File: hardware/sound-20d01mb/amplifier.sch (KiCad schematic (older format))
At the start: 49 parts

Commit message: Added AD1938
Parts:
- removed C?: 10uF, Capacitor_SMD:CP_Elec_4x5.4, symbol Device:CP
- removed C? (x5): 0.1uF, Capacitor_SMD:C_1206_3216Metric_Pad1.42x1.75mm_HandSolder, symbol Device:C
- removed C? (x2): 10uF, Capacitor_THT:CP_Radial_D8.0mm_P3.50mm, symbol Device:CP
- removed R?: 100K, Resistor_SMD:R_1206_3216Metric_Pad1.42x1.75mm_HandSolder, symbol Device:R
- removed R? (x2): 100R, Resistor_SMD:R_1206_3216Metric_Pad1.42x1.75mm_HandSolder, symbol Device:R
- removed R? (x2): 10K, Resistor_SMD:R_1206_3216Metric_Pad1.42x1.75mm_HandSolder, symbol Device:R
- removed U?: PGA2311P, Package_DIP:DIP-16_W7.62mm, symbol sound-20d01_Library:PGA2311P
- removed U?: ADG3304BRUZ, Package_SO:TSSOP-14_4.4x5mm_P0.65mm, symbol sound-20d01_Library:ADG3304BRUZ
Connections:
- net labels removed: +3.3V, +5V, +5VA, -5VA, PGA_SCLK, PGA_SDI, PGA_ZCEN, VOL_SCLK, VOL_SDI, VOL_ZCEN, ~PGA_CS, ~VOL_CS
- wire segments 229 -> 145
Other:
- note removed: "Place power-supply bypass capacitors as\nclose to the PGA2311 package as physically possible."
- moved on the sheet: C?, L?, R?, SW?, U?

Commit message: Updated schematics
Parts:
- removed C?: 10uF, Capacitor_THT:CP_Radial_D8.0mm_P3.50mm, symbol Device:CP
- removed R? (x2): 100R, Resistor_SMD:R_1206_3216Metric_Pad1.42x1.75mm_HandSolder, symbol Device:R
- removed R? (x2): 1M, Resistor_SMD:R_1206_3216Metric_Pad1.42x1.75mm_HandSolder, symbol Device:R
- added C?: 10uF, Capacitor_SMD:C_1210_3225Metric_Pad1.42x2.65mm_HandSolder, symbol Device:C
- C?: value 1uF -> 2.2uF
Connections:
- net GNDA: now also C?.2
- net LIN: now also C?.1
- net RIN: now also C?.1
- net VCC: now also C?.1
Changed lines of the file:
@@
 	5750 3800 5750 4700
-$Comp
-L Device:CP C?
-U 1 1 60E1A09F
-P 6850 2850
-F 0 "C?" H 6968 2896 50  0000 L CNN
-F 1 "10uF" H 6968 2805 50  0000 L CNN
-F 2 "Capacitor_THT:CP_Radial_D8.0mm_P3.50mm" H 6888 2700 50  0001 C CNN
-F 3 "~" H 6850 2850 50  0001 C CNN
-	1    6850 2850
-	1    0    0    -1
-$EndComp
 $Comp
 L Device:C C?
@@
 Wire Wire Line
 	4400 4700 4650 4700
-Wire Wire Line
-	4400 5400 4400 4700
 $Comp
 L Device:C C?
@@
 P 3400 4850
 F 0 "C?" H 3515 4896 50  0000 L CNN
-F 1 "1uF" H 3515 4805 50  0000 L CNN
+F 1 "2.2uF" H 3515 4805 50  0000 L CNN
 F 2 "Capacitor_SMD:C_1206_3216Metric_Pad1.42x1.75mm_HandSolder" H 3438 4700 50  0001 C CNN
 F 3 "~" H 3400 4850 50  0001 C CNN
@@
 	0    -1   -1   0
 $EndComp
-Text HLabel 2300 3700 0    50   Input ~ 0
+Text HLabel 2800 3700 0    50   Input ~ 0
 LIN
-Text HLabel 2300 4600 0    50   Input ~ 0
+Text HLabel 2800 4600 0    50   Input ~ 0
 RIN
 Text HLabel 8550 3600 2    50   Output ~ 0
@@
 Text GLabel 5850 4400 2    50   Input ~ 0
 GAIN1
-$Comp
-L Device:R R?
-U 1 1 60E774AC
-P 2550 3700
-F 0 "R?" V 2757 3700 50  0000 C CNN
-F 1 "100R" V 2666 3700 50  0000 C CNN
-F 2 "Resistor_SMD:R_1206_3216Metric_Pad1.42x1.75mm_HandSolder" V 2480 3700 50  0001 C CNN
-F 3 "~" H 2550 3700 50  0001 C CNN
-	1    2550 3700
-	0    -1   -1   0
-$EndComp
-$Comp
-L Device:R R?
-U 1 1 60E83DCC
-P 2550 4600
-F 0 "R?" V 2757 4600 50  0000 C CNN
-F 1 "100R" V 2666 4600 50  0000 C CNN
-F 2 "Resistor_SMD:R_1206_3216Metric_Pad1.42x1.75mm_HandSolder" V 2480 4600 50  0001 C CNN
-F 3 "~" H 2550 4600 50  0001 C CNN
-	1    2550 4600
-	0    -1   -1   0
-$EndComp
-$Comp
-L power:GNDA #PWR?
-U 1 1 60EDFC4C
-P 2800 5100
-F 0 "#PWR?" H 2800 4850 50  0001 C CNN
-F 1 "GNDA" H 2805 4927 50  0000 C CNN
-F 2 "" H 2800 5100 50  0001 C CNN
-F 3 "" H 2800 5100 50  0001 C CNN
-	1    2800 5100
-	1    0    0    -1
-$EndComp
-Wire Wire Line
-	2800 5000 2800 5100
-$Comp
-L Device:R R?
-U 1 1 60F53986
-P 2800 3950
-F 0 "R?" H 2870 3996 50  0000 L CNN
-F 1 "1M" H 2870 3905 50  0000 L CNN
-F 2 "Resistor_SMD:R_1206_3216Metric_Pad1.42x1.75mm_HandSolder" V 2730 3950 50  0001 C CNN
-F 3 "~" H 2800 3950 50  0001 C CNN
-	1    2800 3950
-	1    0    0    -1
-$EndComp
-$Comp
-L power:GNDA #PWR?
-U 1 1 60F5398D
-P 2800 4200
-F 0 "#PWR?" H 2800 3950 50  0001 C CNN
-F 1 "GNDA" H 2805 4027 50  0000 C CNN
-F 2 "" H 2800 4200 50  0001 C CNN
-F 3 "" H 2800 4200 50  0001 C CNN
-	1    2800 4200
-	1    0    0    -1
-$EndComp
-Wire Wire Line
-	2800 4100 2800 4200
-Wire Wire Line
-	2300 3700 2400 3700
-Wire Wire Line
-	2700 3700 2800 3700
-Wire Wire Line
-	2800 3700 2800 3800
-Connection ~ 2800 3700
 Wire Wire Line
 	2800 3700 2900 3700
@@
 Wire Wire Line
 	3300 4100 4650 4100
-Wire Wire Line
-	2300 4600 2400 4600
-Wire Wire Line
-	2700 4600 2800 4600
-Wire Wire Line
-	2800 4600 2800 4700
-Connection ~ 2800 4600
 Wire Wire Line
 	2800 4600 2900 4600
@@
 	4550 4500 4550 4900
 Connection ~ 5150 4900
-$Comp
-L Device:R R?
-U 1 1 60EBA10D
-P 2800 4850
-F 0 "R?" H 2870 4896 50  0000 L CNN
-F 1 "1M" H 2870 4805 50  0000 L CNN
-F 2 "Resistor_SMD:R_1206_3216Metric_Pad1.42x1.75mm_HandSolder" V 2730 4850 50  0001 C CNN
-F 3 "~" H 2800 4850 50  0001 C CNN
-	1    2800 4850
-	1    0    0    -1
-$EndComp
+Wire Wire Line
+	4400 5400 4400 4700
+$Comp
+L Device:C C?
+U 1 1 613EF0A5
+P 6850 2850
+F 0 "C?" H 6965 2896 50  0000 L CNN
+F 1 "10uF" H 6965 2805 50  0000 L CNN
+F 2 "Capacitor_SMD:C_1210_3225Metric_Pad1.42x2.65mm_HandSolder" H 6888 2700 50  0001 C CNN
+F 3 "~" H 6850 2850 50  0001 C CNN
+	1    6850 2850
+	1    0    0    -1
+$EndComp

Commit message: Added OSC
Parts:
- removed R? (x2): 10K, Resistor_SMD:R_1206_3216Metric_Pad1.42x1.75mm_HandSolder, symbol Device:R
- removed R? (x2): 1K, Resistor_SMD:R_1206_3216Metric_Pad1.42x1.75mm_HandSolder, symbol Device:R
- removed U? (x2): PC817, Package_DIP:DIP-4_W7.62mm, symbol Isolator:PC817
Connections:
- net GNDA: now also U?.3 (MUTE)
- net VCC: now also U?.2 (~SD)
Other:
- moved on the sheet: C?, L?, R?, SW?, U?

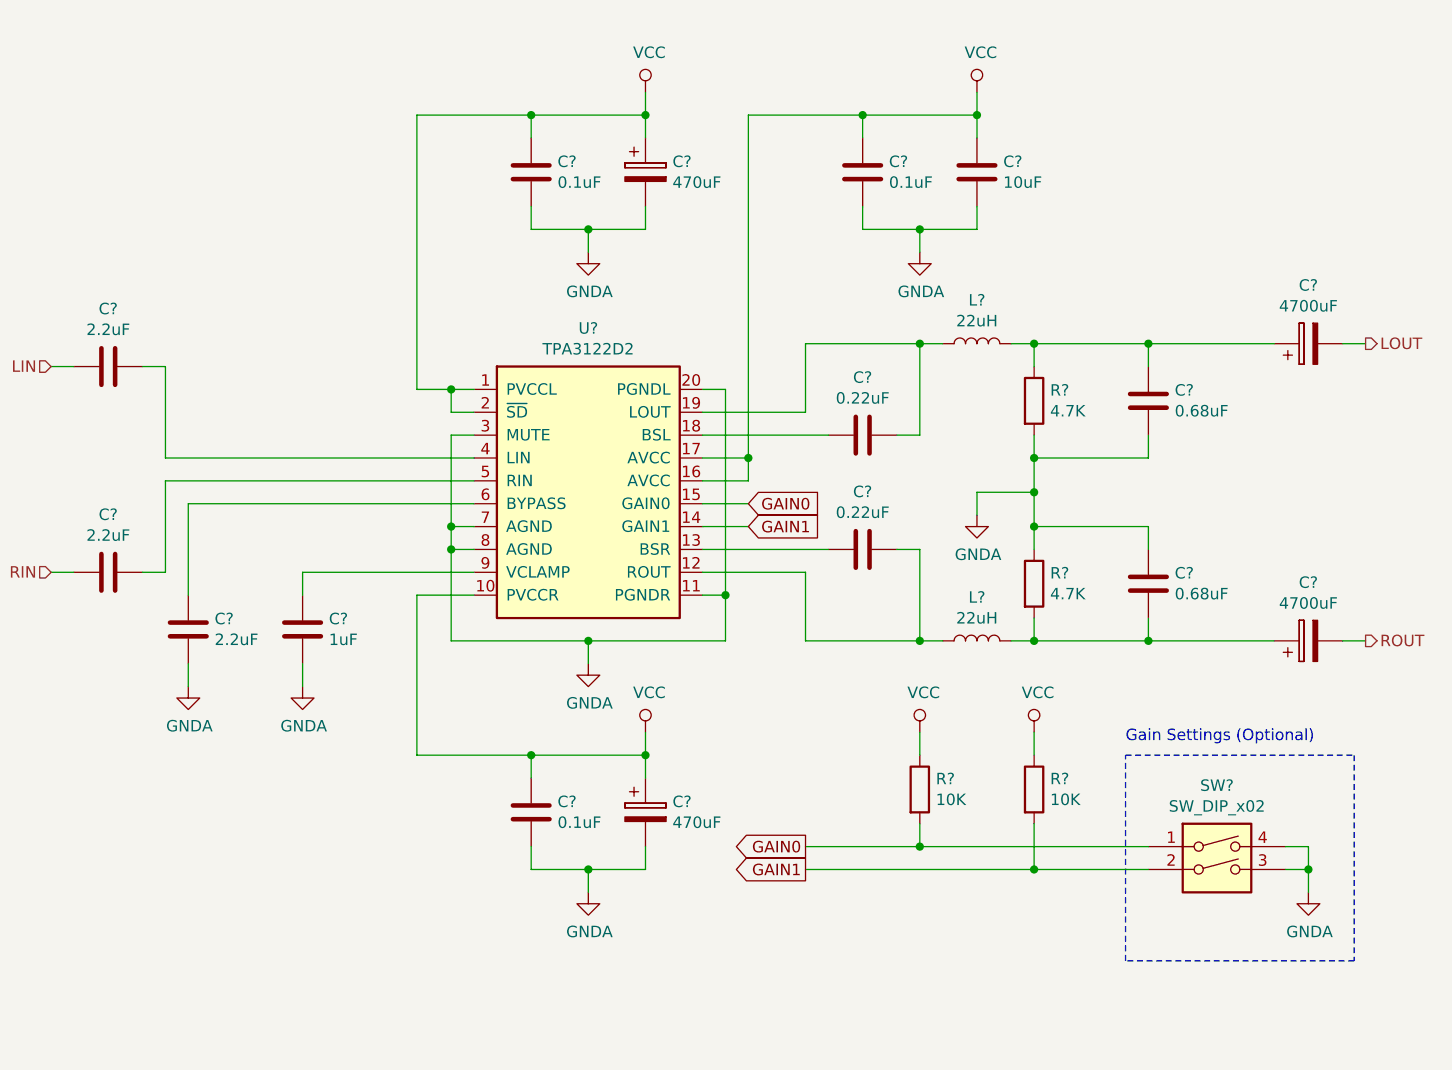
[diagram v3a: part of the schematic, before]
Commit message: New amplifier (TPA3123D2)
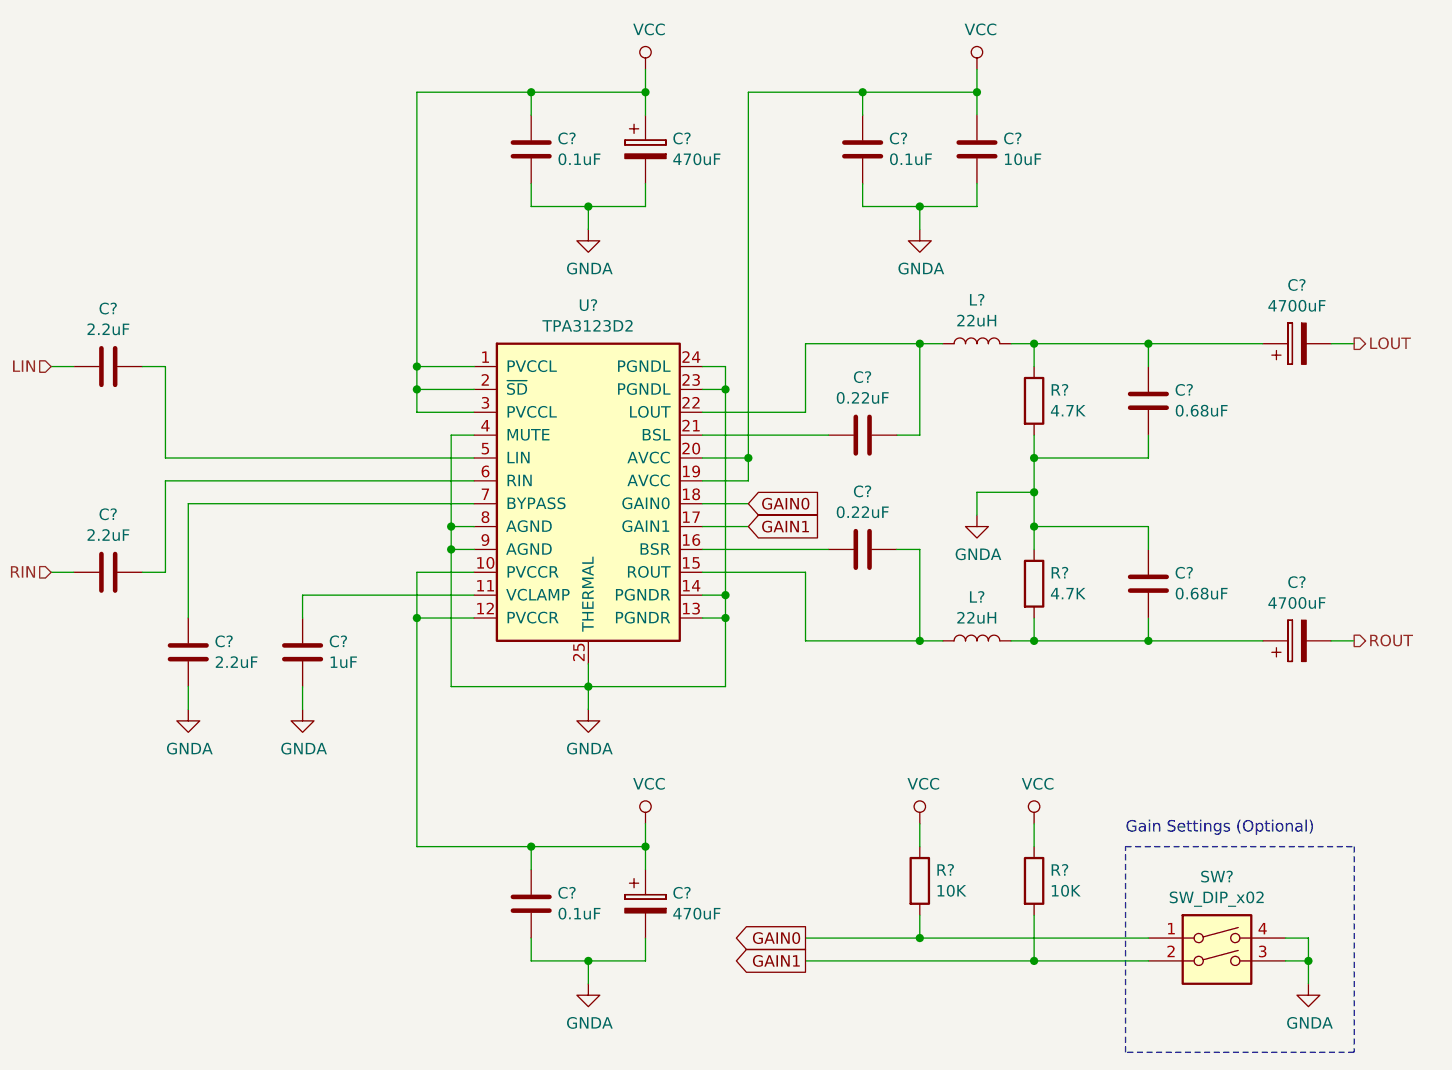
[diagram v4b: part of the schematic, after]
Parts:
- removed U?: TPA3122D2, Package_DIP:DIP-20_W7.62mm, symbol sound-20d01_Library:TPA3122D2
- added U?: TPA3123D2, Package_SO:HTSSOP-24-1EP_4.4x7.8mm_P0.65mm_EP3.4x7.8mm_Mask2.4x4.68mm_ThermalVias, symbol sound-20d01_Library:TPA3123D2
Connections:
- net GAIN0: now also U?.18 (GAIN0)
- net GAIN1: now also U?.17 (GAIN1)
- net GNDA: now also U?.13 (PGNDR), U?.14 (PGNDR), U?.23 (PGNDL), U?.24 (PGNDL), U?.25 (THERMAL), U?.4 (MUTE), U?.8 (AGND), U?.9 (AGND)
- net VCC: now also U?.1 (PVCCL), U?.10 (PVCCR), U?.12 (PVCCR), U?.19 (AVCC), U?.2 (~SD), U?.20 (AVCC), U?.3 (PVCCL)
- net at C?.2, L?.1: now also U?.15 (ROUT)
- net at C?.1: now also U?.16 (BSR)
- net at C?.1: now also U?.21 (BSL)
- net at C?.2, L?.1: now also U?.22 (LOUT)
- net at C?.2: now also U?.5 (LIN)
- net at C?.2: now also U?.6 (RIN)
- net at C?.1: now also U?.7 (BYPASS)
- net at C?.1: now also U?.11 (VCLAMP)
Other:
- moved on the sheet: C?, R?, SW?

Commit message: Added X977B04
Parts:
- C? (x2): footprint (none) -> Capacitor_THT:CP_Radial_D12.5mm_P5.00mm
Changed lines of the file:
@@
 F 0 "C?" H 5518 2146 50  0000 L CNN
 F 1 "470uF" H 5518 2055 50  0000 L CNN
-F 2 "" H 5438 1950 50  0001 C CNN
+F 2 "Capacitor_THT:CP_Radial_D12.5mm_P5.00mm" H 5438 1950 50  0001 C CNN
 F 3 "~" H 5400 2100 50  0001 C CNN
 	1    5400 2100
@@
 F 0 "C?" H 5518 5446 50  0000 L CNN
 F 1 "470uF" H 5518 5355 50  0000 L CNN
-F 2 "" H 5438 5250 50  0001 C CNN
+F 2 "Capacitor_THT:CP_Radial_D12.5mm_P5.00mm" H 5438 5250 50  0001 C CNN
 F 3 "~" H 5400 5400 50  0001 C CNN
 	1    5400 5400

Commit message: Updated schematic
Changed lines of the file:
@@
 	1    0    0    -1
 $EndComp
+Text HLabel 2800 1700 0    50   Input ~ 0
+~SHUTDOWN
+Text HLabel 2800 1800 0    50   Input ~ 0
+MUTE
 $EndSCHEMATC

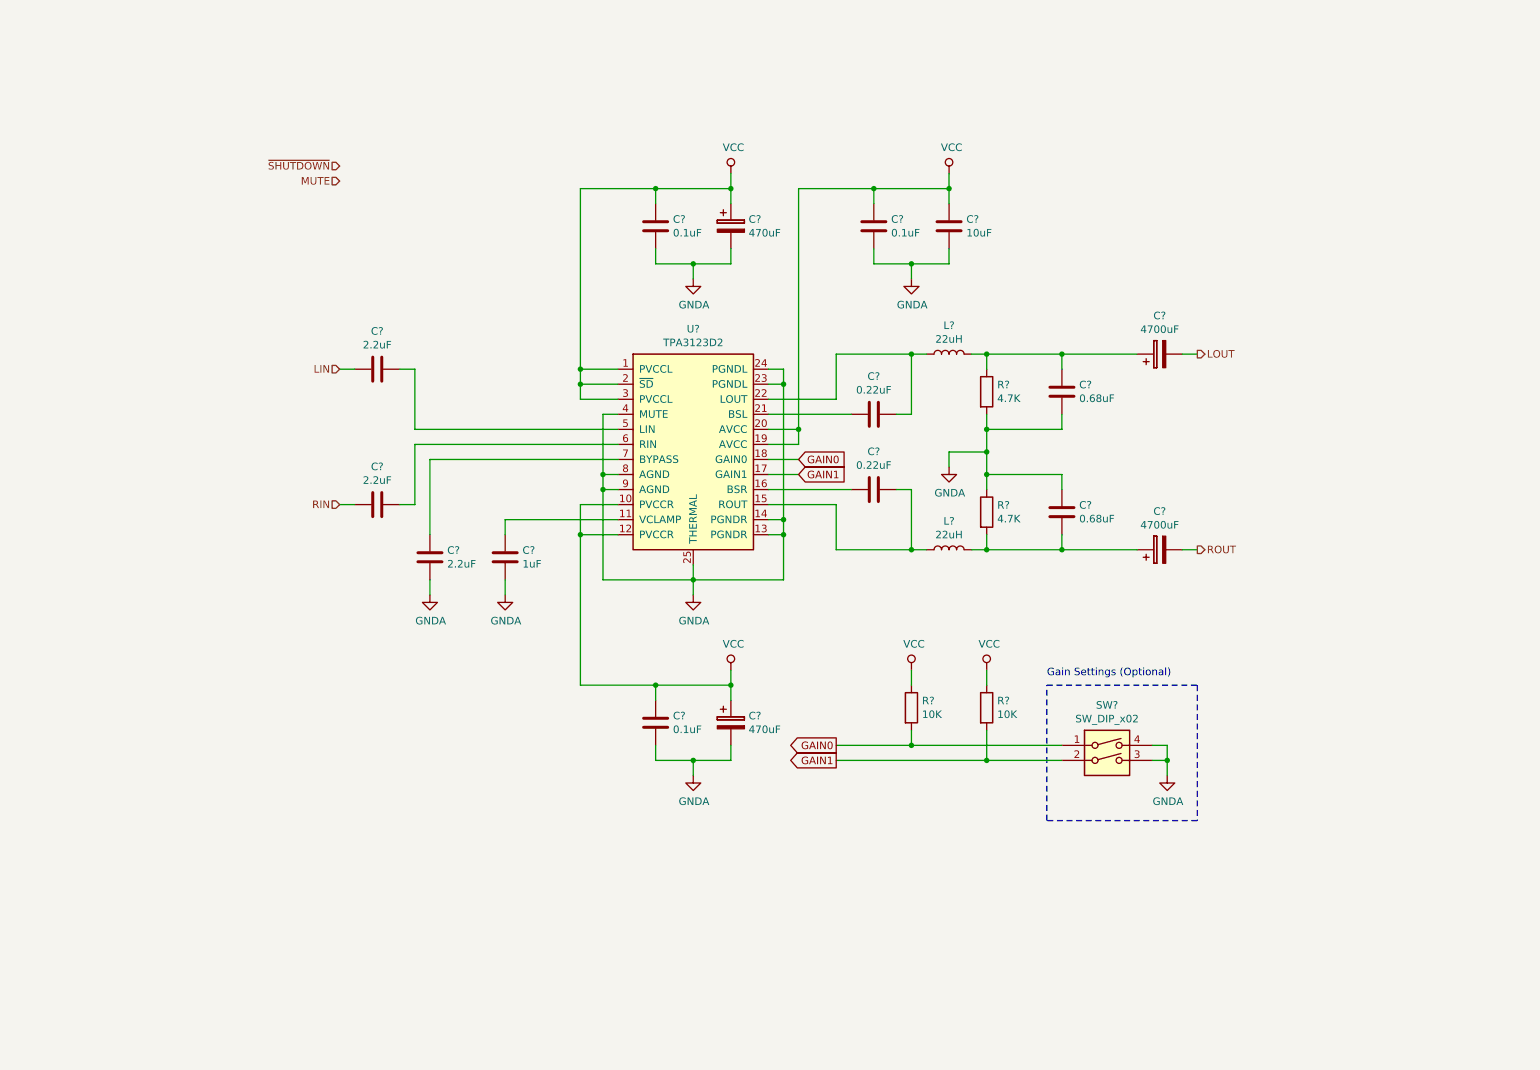
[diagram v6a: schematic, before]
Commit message: Added SD and MUTE to schematic
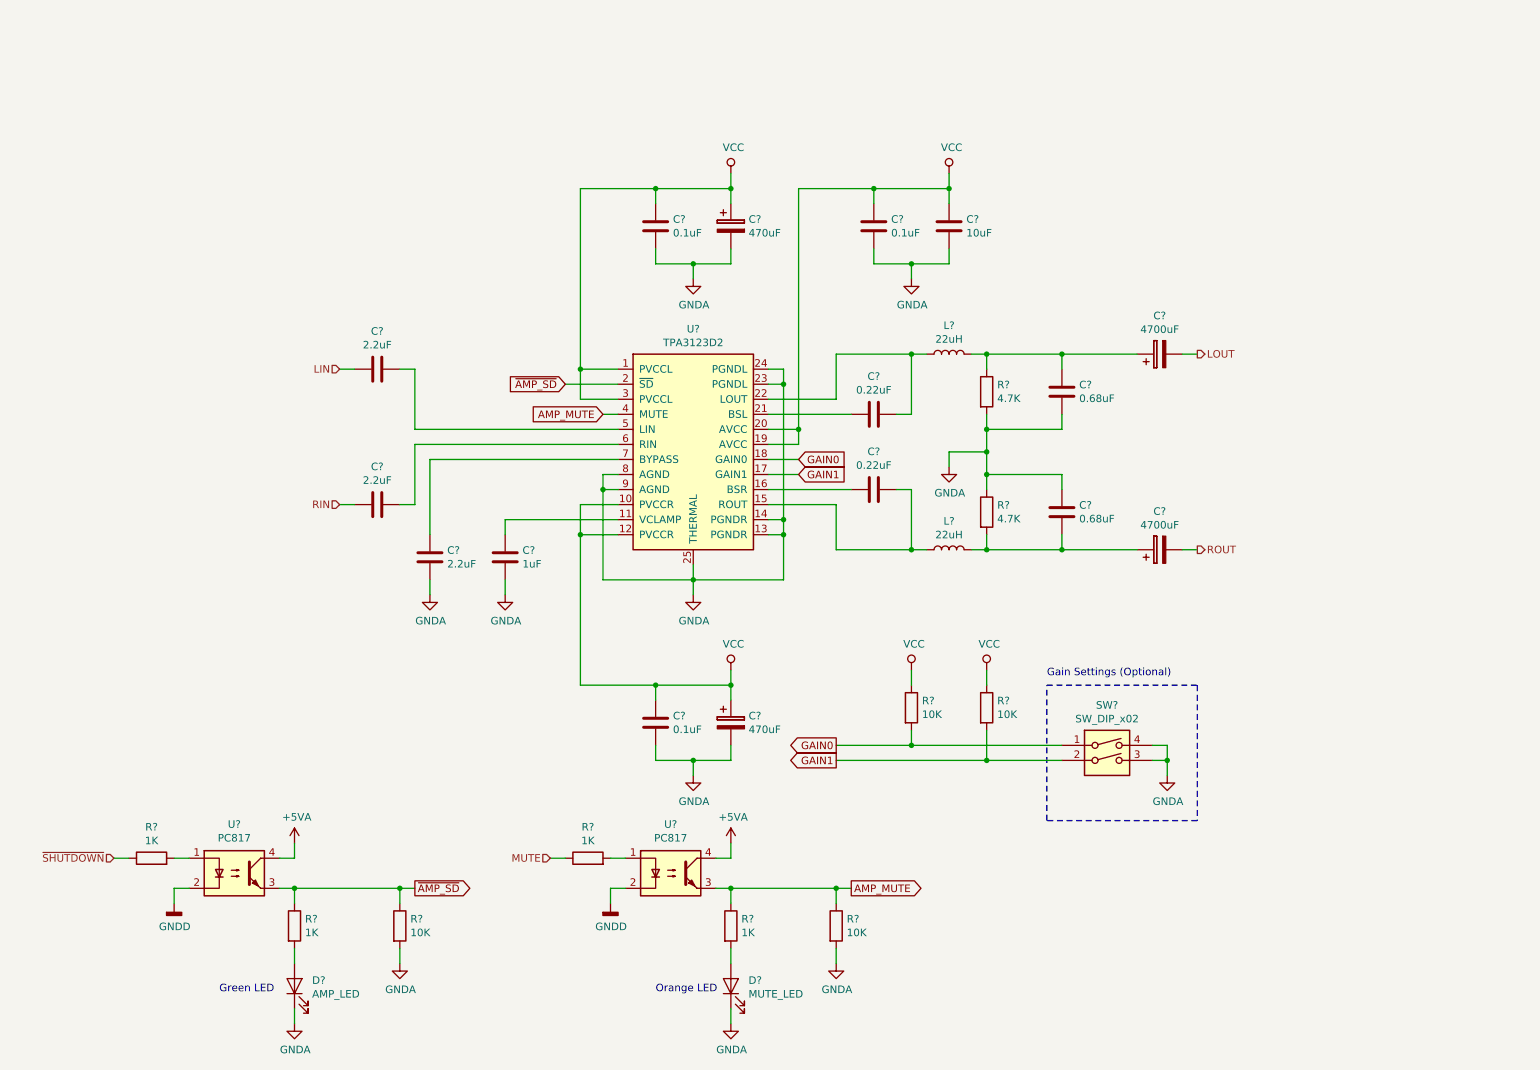
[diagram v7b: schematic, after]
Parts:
- added D?: MUTE_LED, LED_SMD:LED_1206_3216Metric_Pad1.42x1.75mm_HandSolder, symbol Device:LED
- added D?: AMP_LED, LED_SMD:LED_1206_3216Metric_Pad1.42x1.75mm_HandSolder, symbol Device:LED
- added R? (x4): 1K, Resistor_SMD:R_1206_3216Metric_Pad1.42x1.75mm_HandSolder, symbol Device:R
- added R? (x2): 10K, Resistor_SMD:R_1206_3216Metric_Pad1.42x1.75mm_HandSolder, symbol Device:R
- added U? (x2): PC817, Package_DIP:DIP-4_W7.62mm, symbol Isolator:PC817
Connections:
- net GNDA: now also D?.1 (K), D?.1 (K), R?.2, R?.2; no longer U?.4 (MUTE)
- net MUTE: now also R?.1
- net VCC: no longer U?.2 (~SD)
- net ~SHUTDOWN: now also R?.1
- new net: R?.2, U?.1 (x2)
- new net: D?.2 (A), R?.2 (x2)
- new net +5VA: U?.4, U?.4
- new net AMP_MUTE: R?.1, R?.1, U?.3, U?.4 (MUTE)
- new net GNDD: U?.2, U?.2
- new net ~AMP_SD: R?.1, R?.1, U?.2 (~SD), U?.3
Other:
- note added: "Green LED"
- note added: "Orange LED"
